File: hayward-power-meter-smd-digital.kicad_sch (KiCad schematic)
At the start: 31 parts, among them J1 Conn_Coaxial, J2 Conn_Coaxial, SW1 SW_SPST, U1 LM358, U2 LM78L05_SO8, U3 AD8310ARMZ

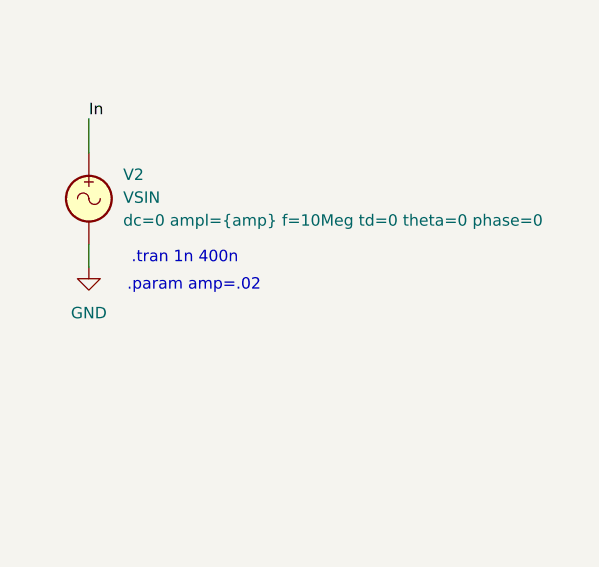
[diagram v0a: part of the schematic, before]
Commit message: New LtSpice Sim with  AD8541
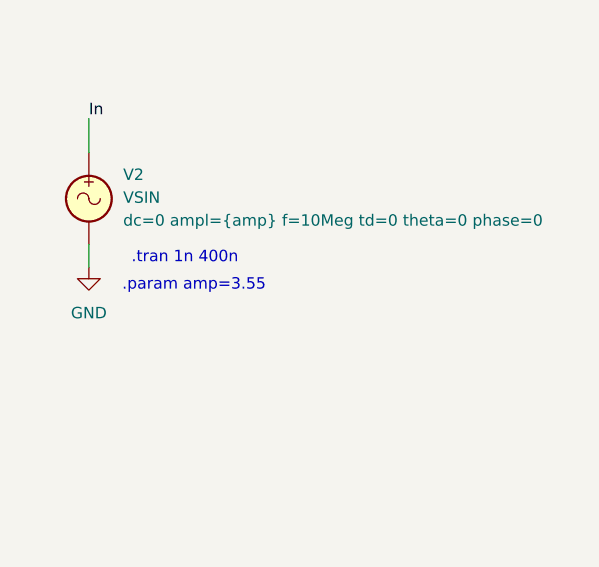
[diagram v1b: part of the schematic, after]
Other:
- note added: ".param amp=3.55"
- note removed: ".param amp=.02"
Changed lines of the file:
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@@
 		)
 	)
-	(text ".param amp=.02"
+	(text ".param amp=3.55"
 		(exclude_from_sim no)
 		(at 42.164 167.132 0)
